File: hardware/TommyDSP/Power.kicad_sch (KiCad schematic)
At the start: 29 parts, among them J401 Conn_01x02_Pin, Q401 AO3401A, U401 TPS7A2033PDBVR, U402 TPS62A01APDDC, U403 TP4056-42-ESOP8

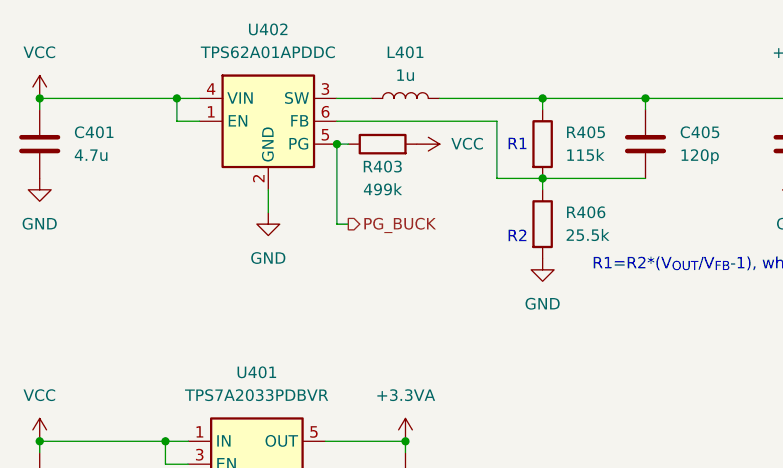
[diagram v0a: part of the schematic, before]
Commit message: bump to KiCad V10, add logo
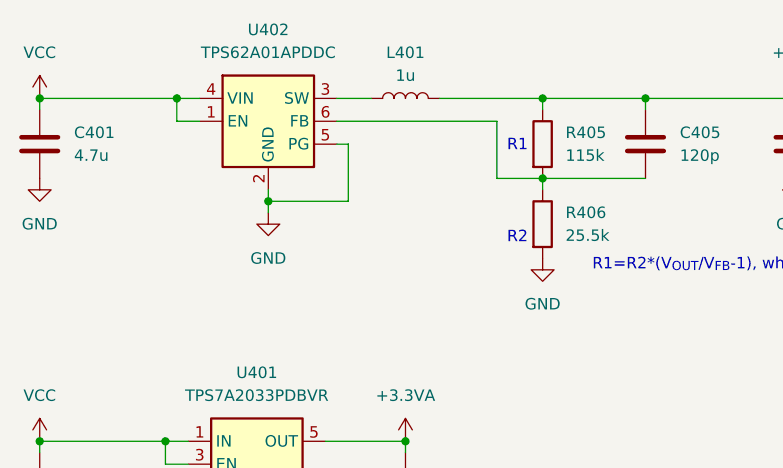
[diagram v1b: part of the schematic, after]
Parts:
- removed R403: 499k, Resistor_SMD:R_0603_1608Metric, symbol Device:R
- JP401: now left out of the parts list
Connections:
- net PG_BUCK is gone; now on net GND: U402.5 (PG)
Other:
- title: Power -> TommyDSP
